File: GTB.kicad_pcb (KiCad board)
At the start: 2 copper layers, 32 x 29 mm, 9 parts, among them U1 7555-S08N

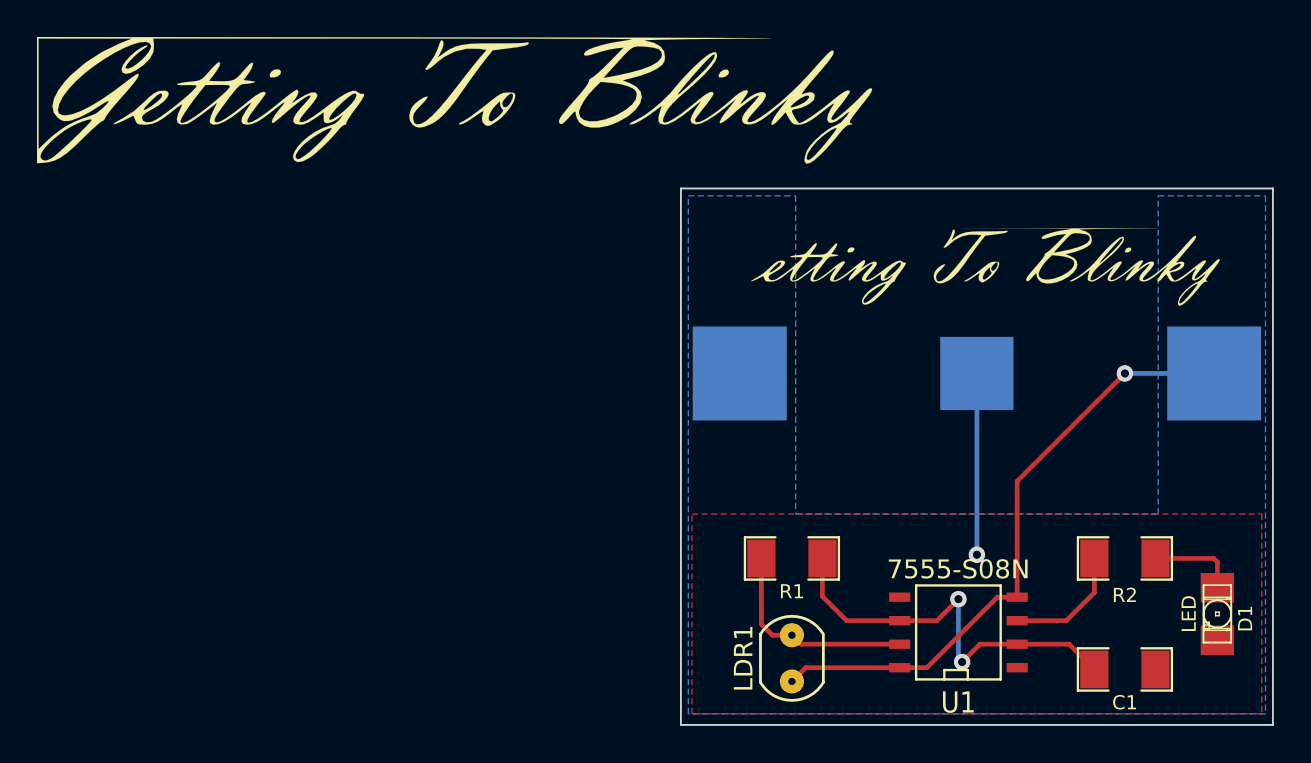
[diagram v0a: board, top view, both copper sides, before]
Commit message: Finally finished GTB
Getting To Blinky board finally finished. The Solder mask relief is a
bit grainy though. Needs a higher resolution bitmap.
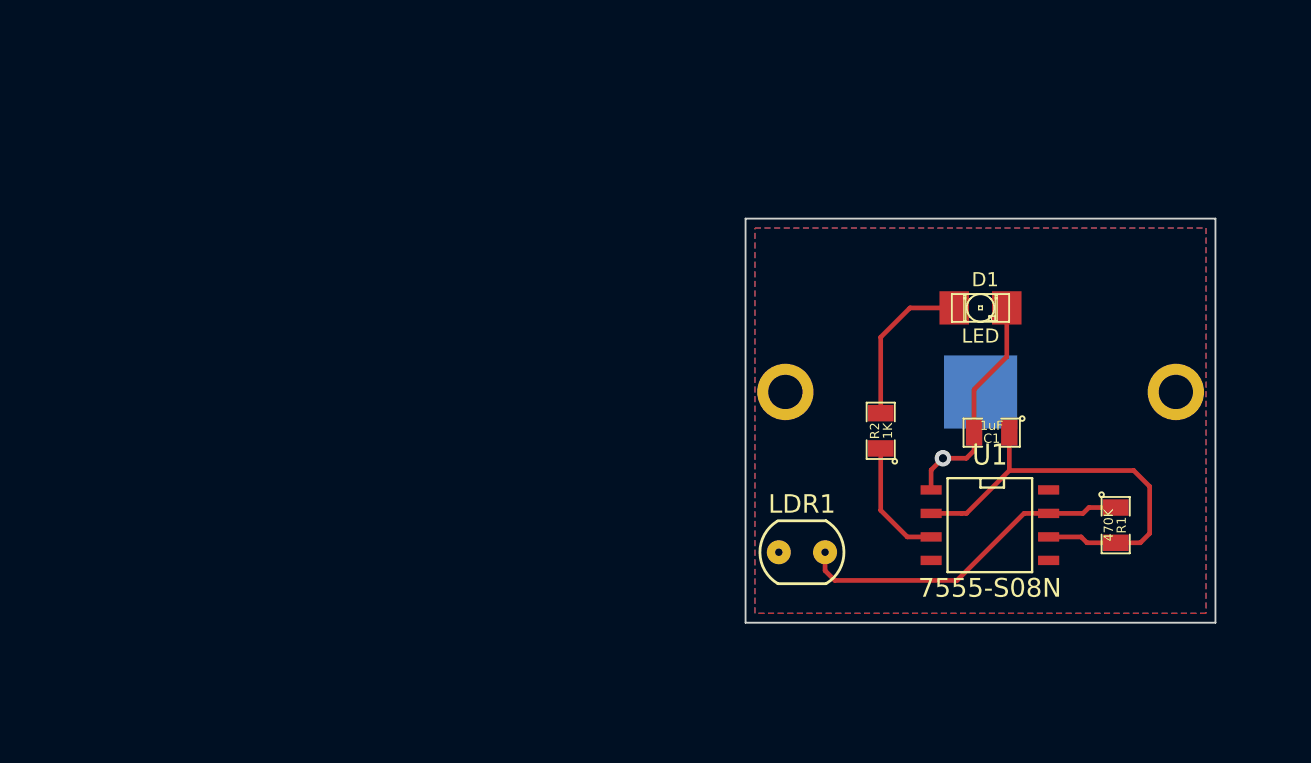
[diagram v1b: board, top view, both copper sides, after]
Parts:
- removed G***: LOGO, LOGO
- removed the VAL at (154.2, 90.2)
- added VAL: ScriptScript3, ScriptScript3, F.Cu at (155.2, 90.2)
- BAT1: footprint CR2032_Holder -> CR2032_Holder_ThruHole
- C1, R1, R2: footprint SM1206 -> SM0805
- moved D1 20.9 mm to (155.2, 92.5), turned to 0 degrees
- moved R1 17.6 mm to (162.5, 104.2), turned to 270 degrees
- moved R2 14.9 mm to (149.8, 99.1), turned to 90 degrees
- moved C1 14.7 mm to (155.8, 99.2), turned to 180 degrees
- moved U1 6.04 mm to (155.7, 104.2), turned to 270 degrees
- moved LDR1 5.76 mm to (145.5, 105.7), turned to 0 degrees
- moved BAT1 1.02 mm to (155.2, 97.0)
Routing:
- net VCC: track 33.4 -> 0.00 mm, vias 1 -> 0
- net /Discharge: track 11.5 -> 18.6 mm
- net N-000007: track 4.81 -> 8.74 mm
- net GND: track 9.80 -> 12.3 mm
- net /Trigger: track 22.0 -> 23.5 mm, vias 2 -> 0
- added copper zone on B.Cu, net GND
- added copper zone on F.Cu, net VCC
- removed copper zone on F.Cu, net GND
- removed copper zone on B.Cu, net VCC
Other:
- board size 32 x 29 mm -> 25.4 x 21.8 mm
